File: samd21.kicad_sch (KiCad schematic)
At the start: 42 parts, among them J5 S4B-ZR-SM4A-TF(LF)(SN), J6 S6B-ZR-SM4A-TF(LF)(SN), Q1 DTC043ZEB, Q2 DTC043ZEB, Q3 DTC043ZEB, SW1 SW_Push, SW2 SW_Push, U1 ATSAMD21J18A-M, U2 TXS0108EPW, Y1 MS1V-T1K_32768

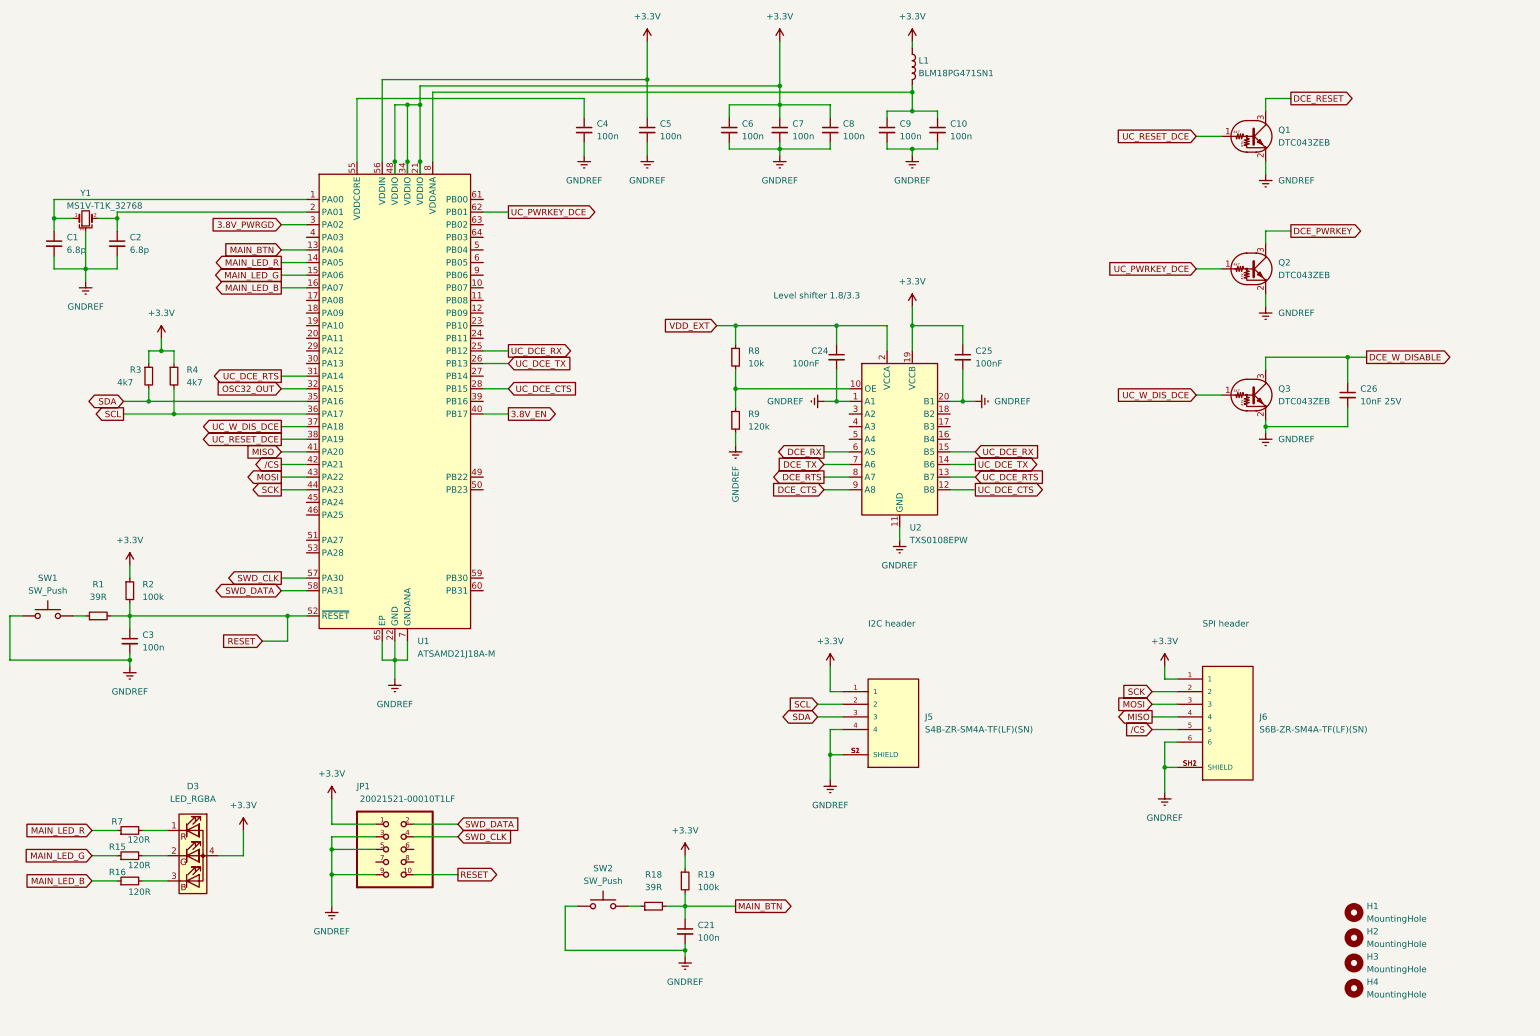
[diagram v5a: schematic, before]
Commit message: Added IO and debug UART to pin header
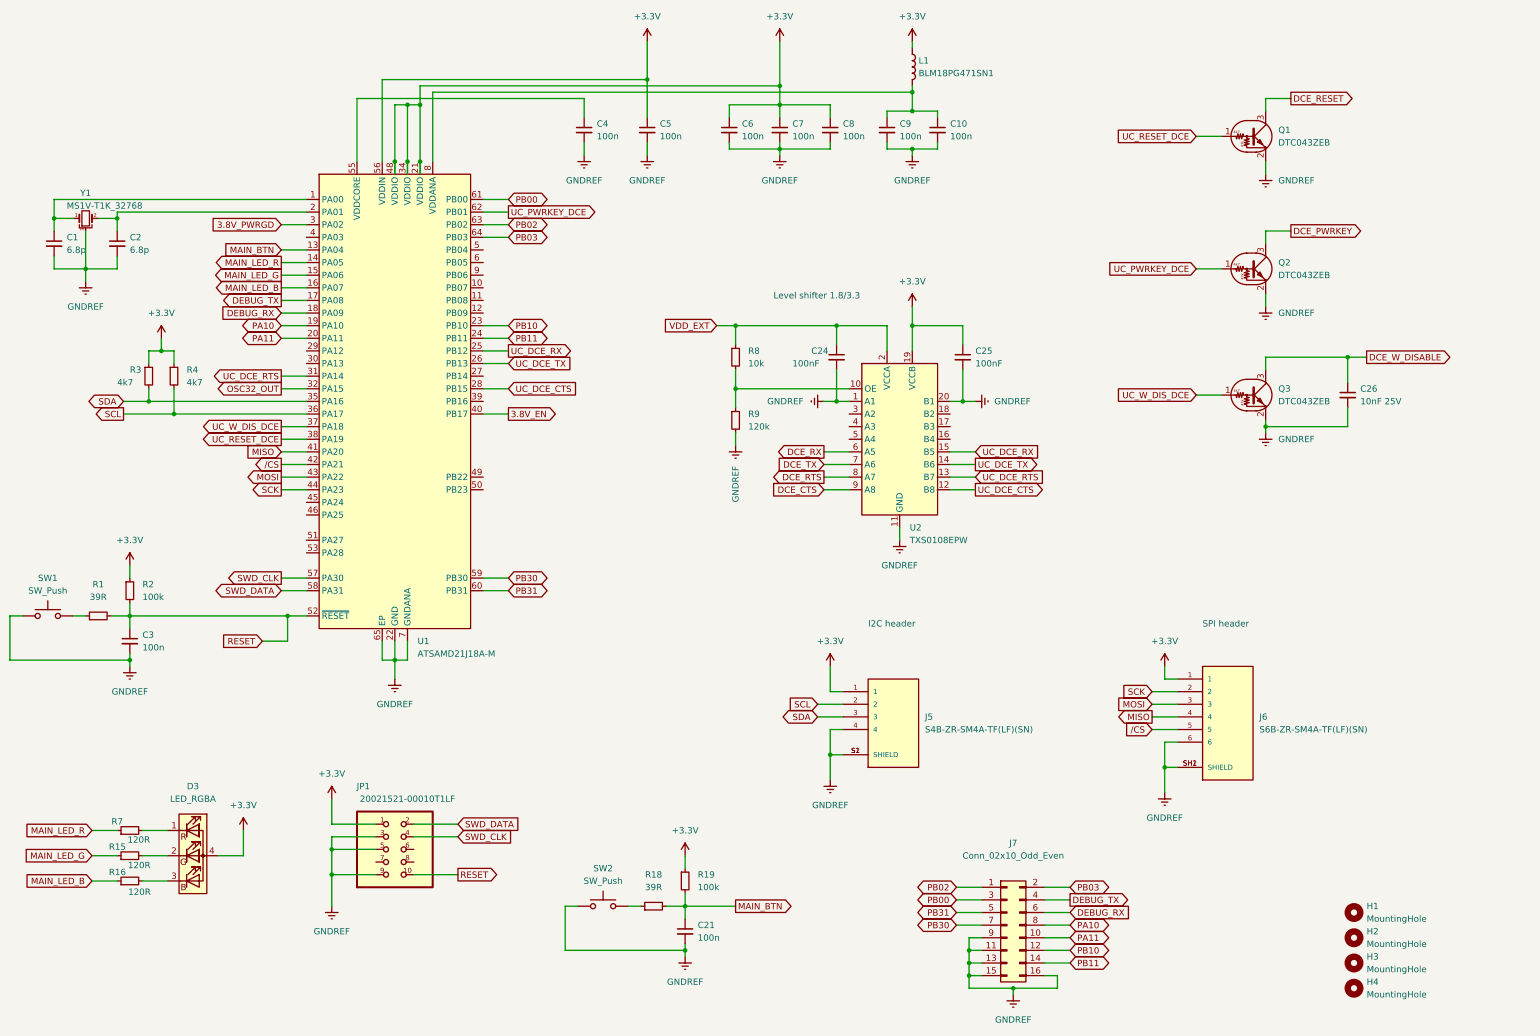
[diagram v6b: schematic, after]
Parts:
- added J7: Conn_02x10_Odd_Even, Connector_PinHeader_2.54mm:PinHeader_2x08_P2.54mm_Vertical, symbol Connector_Generic:Conn_02x08_Odd_Even
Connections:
- net GNDREF: now also J7.11 (Pin_11), J7.13 (Pin_13), J7.15 (Pin_15), J7.16 (Pin_16), J7.9 (Pin_9)
- net DEBUG_TX: now reaches U1.17 (PA08)
- net DEBUG_TX: now also J7.4 (Pin_4)
- net DEBUG_RX: now reaches U1.18 (PA09)
- net DEBUG_RX: now also J7.6 (Pin_6)
- net PA10: now reaches U1.19 (PA10)
- net PA10: now also J7.8 (Pin_8)
- net PA11: now reaches U1.20 (PA11)
- net PA11: now also J7.10 (Pin_10)
- net PB10: now reaches U1.23 (PB10)
- net PB10: now also J7.12 (Pin_12)
- net PB11: now reaches U1.24 (PB11)
- net PB11: now also J7.14 (Pin_14)
- net PB30: now reaches U1.59 (PB30)
- net PB30: now also J7.7 (Pin_7)
- net PB31: now reaches U1.60 (PB31)
- net PB31: now also J7.5 (Pin_5)
- net PB00: now reaches U1.61 (PB00)
- net PB00: now also J7.3 (Pin_3)
- net PB02: now reaches U1.63 (PB02)
- net PB02: now also J7.1 (Pin_1)
- net PB03: now reaches U1.64 (PB03)
- net PB03: now also J7.2 (Pin_2)
